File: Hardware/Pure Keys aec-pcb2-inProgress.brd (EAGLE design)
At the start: 99 x 98.7 mm, 56 parts, among them IC1 TL074P, IC5 TL074P, Q2 20MHz, T1 2N3904, U2 LM4040A50IDBZT, U3 328P

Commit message: updated in progress board added text layer text added classes for power rerouted
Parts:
- U2: value LM4040A50IDBZT -> LM4040
- moved C11 24.7 mm to (86.4, 66.0)
- moved C13 22.9 mm to (80.0, 71.1)
- moved U2 22.2 mm to (91.4, 71.1), turned to 90 degrees
- moved R4 22.2 mm to (25.4, 59.7), turned to 180 degrees
- moved C9 21.6 mm to (80.0, 66.0)
- moved IC1 21.6 mm to (31.8, 26.7)
- moved C5 20.7 mm to (47.0, 30.5)
- moved C14 19.3 mm to (31.8, 63.5)
- moved IC5 17.8 mm to (62.2, 26.7)
- moved C10 17.8 mm to (19.1, 71.1)
- moved V2 15.3 mm to (57.1, 72.4), turned to 180 degrees
- moved R21 15.3 mm to (69.8, 86.4)
- moved R3 15.2 mm to (91.4, 62.2), turned to 180 degrees
- moved C3 14.2 mm to (30.5, 49.5)
- moved R5 14.2 mm to (86.4, 22.9)
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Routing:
- net 5V: track 503.4 -> 412.2 mm, vias 0 -> 8
- net BUT2: track 27.9 -> 86.4 mm
- net GND: track 694.7 -> 641.9 mm, vias 2 -> 3
- net A1IN: track 60.0 -> 10.9 mm
- net A2IN: track 59.7 -> 10.8 mm, vias 1 -> 0
- net MK1: track 89.1 -> 41.2 mm, vias 0 -> 1
- net SCK: track 141.0 -> 99.1 mm, vias 1 -> 3
- net A0IN: track 50.3 -> 10.8 mm, vias 1 -> 0
- net MK0: track 80.1 -> 43.8 mm
- net ENOUT: track 50.5 -> 16.4 mm
- net TRIG1: track 59.8 -> 32.9 mm, vias 1 -> 0
- net N$4: track 74.9 -> 48.5 mm
- net 3VREF: track 45.8 -> 71.4 mm, vias 0 -> 1
- net MOSI: track 129.3 -> 103.8 mm, vias 0 -> 1
- net DAIN: track 41.3 -> 18.4 mm
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- removed copper zone on layer 1, net GND

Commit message: updated board and tests
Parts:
- IC1, IC5: value TL074P -> MCP6004P; device GMSN:DIL14 -> GMSN-R2Project:DIL14
- U$4: value M10X22X10_LOCK -> KeyBoard Connector
- moved ISP1 50.3 mm to (92.7, 54.6)
- moved R21 19.3 mm to (52.1, 94.0)
- moved R22 12.0 mm to (52.1, 88.9)
- moved U$4 6.48 mm to (33.0, 92.7)
- moved BUT1 6.35 mm to (61.0, 92.7)
- moved C7 5.68 mm to (90.2, 47.0), turned to 270 degrees
- moved R17 5.24 mm to (41.9, 83.8)
- moved R19 5.24 mm to (27.9, 83.8)
- moved R20 5.24 mm to (21.6, 83.8)
- moved R18 5.24 mm to (34.3, 83.8)
- moved R3 5.24 mm to (86.4, 61.0)
- moved R16 2.84 mm to (48.3, 83.8)
- moved C6 1.27 mm to (80.0, 57.1)
- moved C8 1.27 mm to (80.0, 52.1)
- moved GLIDE1 1.27 mm to (91.4, 88.9)
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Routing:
- net GND: track 641.9 -> 614.0 mm, vias 3 -> 6
- net 5V: track 412.2 -> 439.9 mm, vias 8 -> 3
- net BUT2: track 86.4 -> 59.7 mm
- net T2: track 38.0 -> 63.6 mm, vias 1 -> 0
- net T7: track 61.1 -> 36.3 mm, vias 1 -> 0
- net MISO: track 53.5 -> 29.5 mm
- net BUTLED1: track 56.8 -> 40.9 mm, vias 0 -> 1
- net T3: track 46.6 -> 62.5 mm, vias 0 -> 1
- net T6: track 50.9 -> 35.8 mm, vias 2 -> 0
- net POT1: track 61.2 -> 49.3 mm
- net MK2: track 35.2 -> 46.9 mm
- net CS2: track 35.1 -> 46.5 mm
- net MK0: track 43.8 -> 53.5 mm, vias 1 -> 0
- net N$7: track 59.5 -> 50.7 mm
- net A1OUT: track 49.5 -> 41.9 mm
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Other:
- board text added: "Pure Keys Dev Board PCB 2 AEC"
- board text removed: "Pure Keys Dev Board V0.2 AEC"

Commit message: changed 74238 for 74138
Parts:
- V1: value 74238N -> 74138N
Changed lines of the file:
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@@
 <attribute name="PROD_ID" value="IC-09136" x="54.61" y="57.15" size="1.778" layer="27" display="off"/>
 </element>
-<element name="V1" library="74ttl-din" library_urn="urn:adsk.eagle:library:84" package="DIL16" package3d_urn="urn:adsk.eagle:package:1462/1" value="74238N" x="34.29" y="72.39"/>
+<element name="V1" library="74ttl-din" library_urn="urn:adsk.eagle:library:84" package="DIL16" package3d_urn="urn:adsk.eagle:package:1462/1" value="74138N" x="34.29" y="72.39"/>
 <element name="V2" library="74ttl-din" library_urn="urn:adsk.eagle:library:84" package="DIL16" package3d_urn="urn:adsk.eagle:package:1462/1" value="74151N" x="57.15" y="72.39" rot="R180"/>
 <element name="R4" library="rcl" package="R0805" value="10K" x="25.4" y="59.69" rot="R180"/>

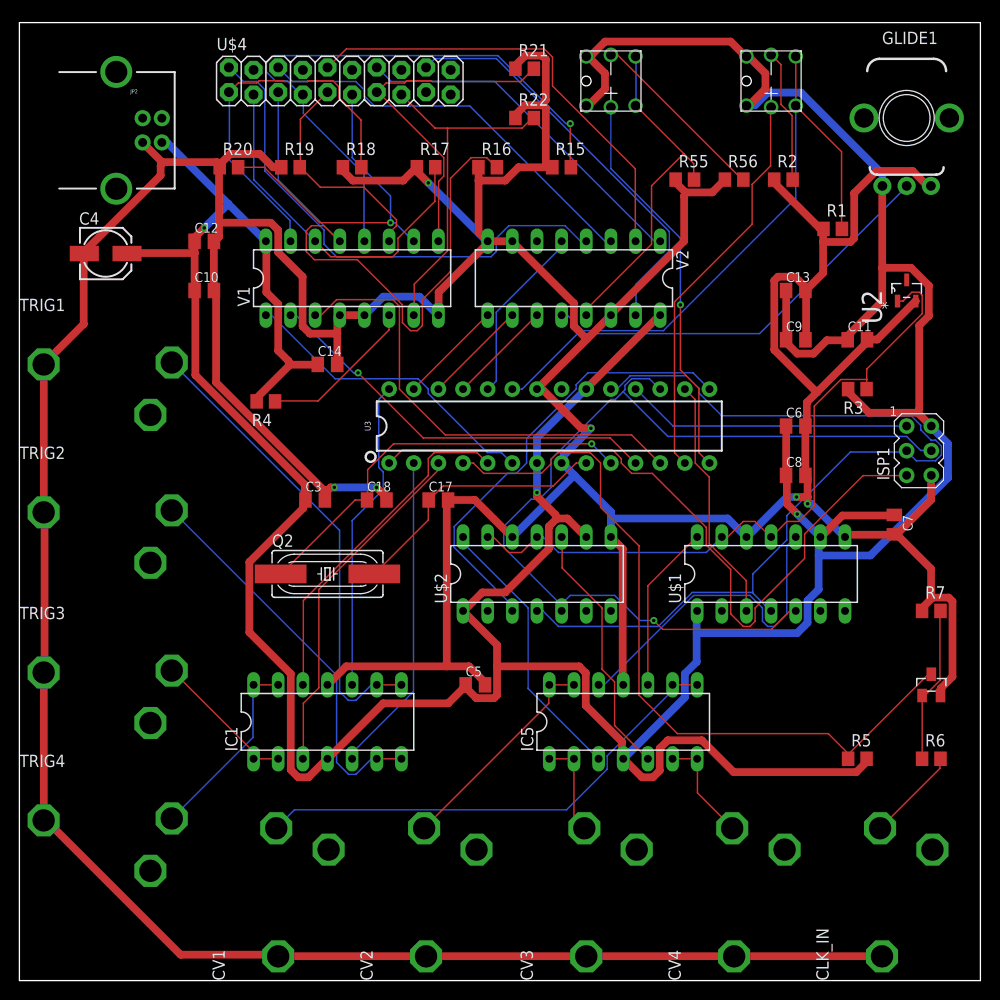
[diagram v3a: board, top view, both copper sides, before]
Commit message: updated switches on in progress
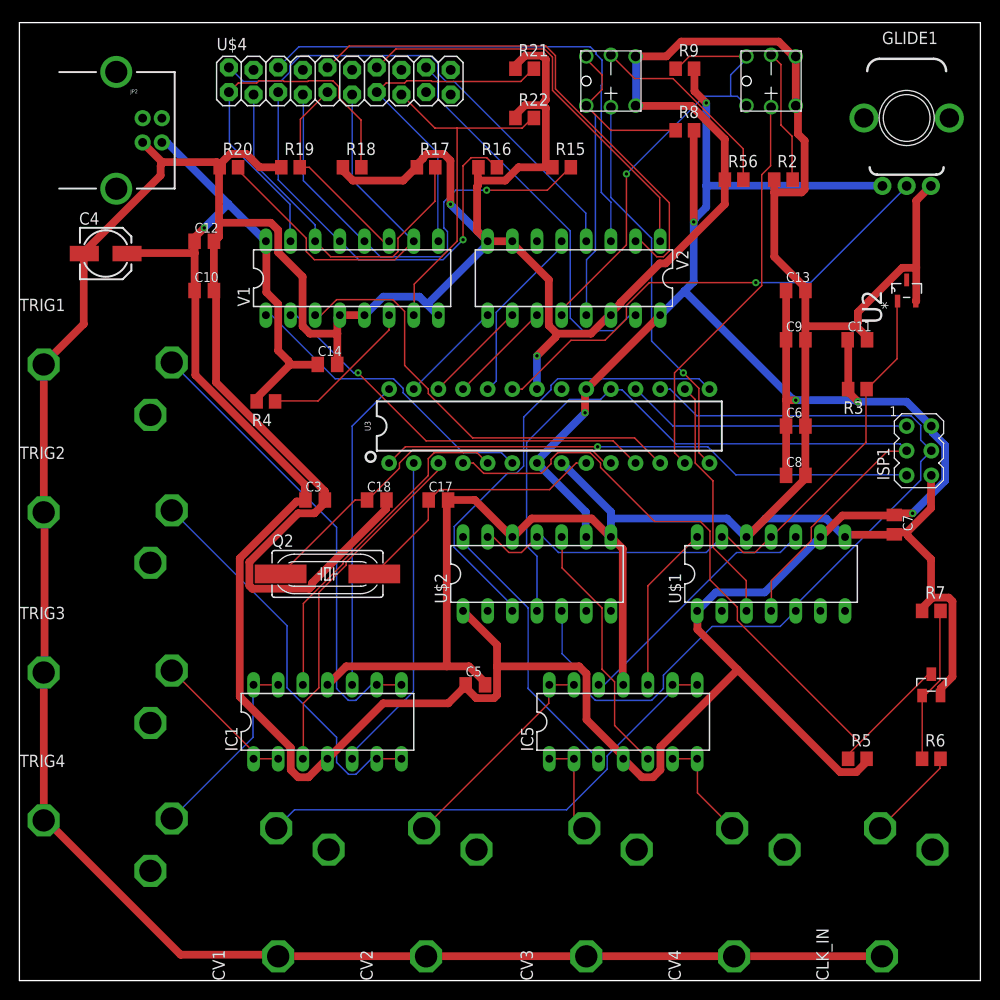
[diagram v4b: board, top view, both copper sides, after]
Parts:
- removed R1, R55: 100K, rcl:R0805
- added R8, R9: 100K, rcl:R0805
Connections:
- net 5V: now also R8.2, R9.2; no longer BUT1.3, BUT1.4, BUT2.3, BUT2.4
- net BUT1: now also BUT1.3, BUT1.4, R8.1; no longer BUT1.1, BUT1.2, R55.2
- net BUT2: now also BUT2.3, BUT2.4, R9.1; no longer BUT2.1, BUT2.2, R1.2
- net GND: now also BUT1.1, BUT1.2, BUT2.1, BUT2.2; no longer R1.1, R55.1
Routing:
- net GND: track 614.0 -> 672.2 mm, vias 6 -> 2
- net 5V: track 439.9 -> 395.9 mm, vias 3 -> 7
- net T2: track 63.6 -> 44.2 mm, vias 0 -> 1
- net RST: track 74.2 -> 55.3 mm, vias 0 -> 1
- net T3: track 62.5 -> 47.0 mm
- net BUT2: track 59.7 -> 46.1 mm, vias 0 -> 1
- net MK1: track 42.1 -> 54.0 mm
- net SCK: track 95.0 -> 85.4 mm
- net MOSI: track 97.8 -> 89.7 mm, vias 1 -> 0
- net 3VREF: track 70.9 -> 63.0 mm
- net VOUTB: track 34.2 -> 26.6 mm
- net CLK_IN: track 78.8 -> 71.3 mm
- net MK2: track 46.9 -> 54.2 mm
- net MK3: track 36.7 -> 42.8 mm
- net T5: track 36.1 -> 41.6 mm, vias 1 -> 0
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
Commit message: Updated routing on in-progress board to make room for 1K pull downs
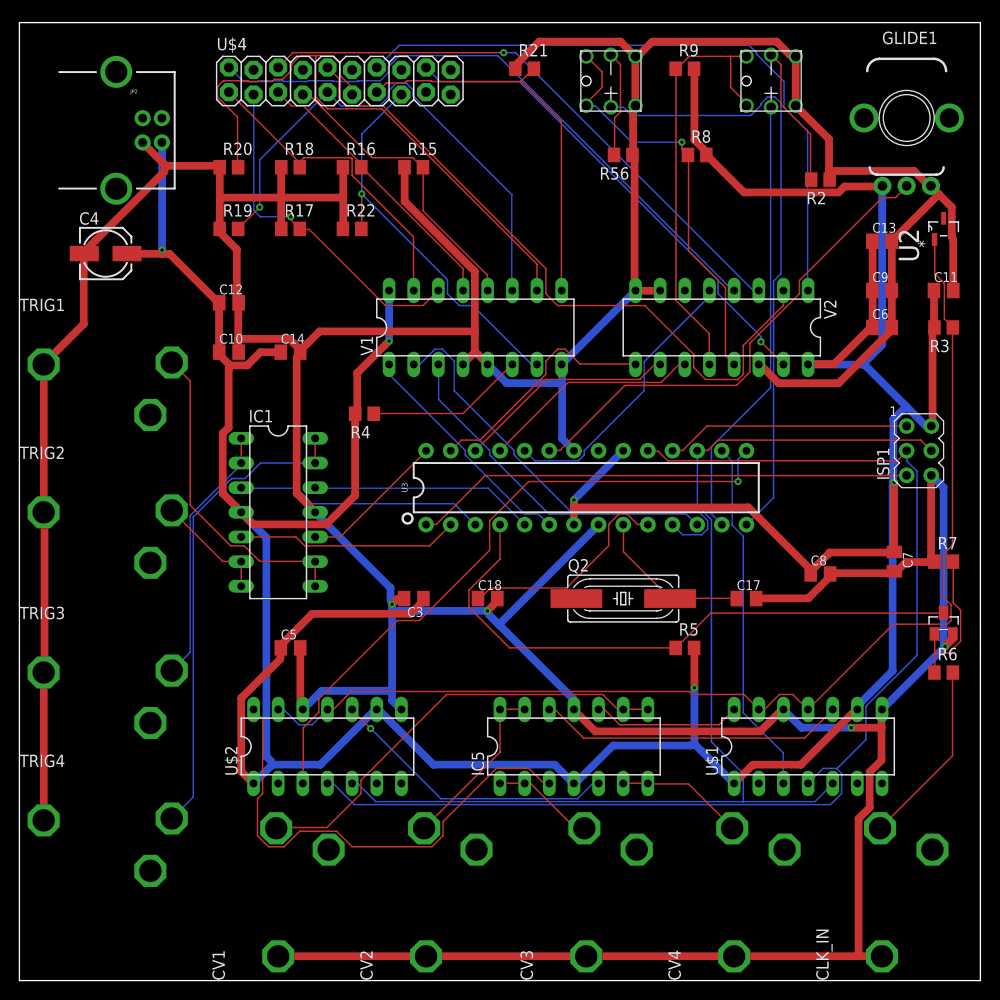
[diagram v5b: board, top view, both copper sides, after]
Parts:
- moved C17 33.3 mm to (74.9, 39.4)
- moved Q2 30.6 mm to (62.2, 39.4)
- moved U$2 28.0 mm to (31.8, 24.1)
- moved IC1 22.2 mm to (26.7, 48.3), turned to 270 degrees
- moved R22 21.1 mm to (34.3, 77.5)
- moved R5 21.1 mm to (68.6, 34.3)
- moved C5 19.4 mm to (27.9, 34.3)
- moved U$1 18.2 mm to (81.3, 24.1)
- moved V2 16.1 mm to (72.4, 67.3)
- moved R17 15.3 mm to (27.9, 77.5)
- moved C18 15.3 mm to (48.3, 39.4)
- moved R15 15.2 mm to (40.6, 83.8)
- moved C3 14.4 mm to (40.6, 39.4), turned to 180 degrees
- moved R16 14.0 mm to (34.3, 83.8)
- moved V1 13.7 mm to (47.0, 67.3)
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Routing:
- net GND: track 672.2 -> 616.6 mm, vias 2 -> 4
- net 3VREF: track 63.0 -> 118.1 mm
- net SCK: track 85.4 -> 125.0 mm
- net T4: track 21.3 -> 53.9 mm, vias 0 -> 1
- net N$5: track 19.8 -> 49.4 mm
- net N$3: track 40.9 -> 11.9 mm
- net MOSI: track 89.7 -> 114.3 mm
- net MK3: track 42.8 -> 67.1 mm
- net BUTLED1: track 40.9 -> 64.0 mm, vias 1 -> 0
- net T5: track 41.6 -> 64.5 mm
- net VOUTC: track 28.7 -> 50.3 mm
- net 5V: track 395.9 -> 416.2 mm, vias 7 -> 5
- net CS2: track 47.5 -> 67.2 mm, vias 0 -> 1
- net TRIG1: track 32.1 -> 15.1 mm
- net T3: track 47.0 -> 30.9 mm, vias 1 -> 0
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
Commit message: changed in progress board
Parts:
- added R1, R10, R11, R12, R13: 1K, rcl:R0805
- R3: value 10K -> 2K
- U2: device GMSN:SOT95P237X112-3N -> GMSN-R2Project:SOT95P237X112-3N
- V1: value 74138N -> 74238N
- moved C11 37.4 mm to (88.9, 34.3)
- moved U2 36.6 mm to (82.5, 43.2)
- moved R3 35.4 mm to (82.5, 34.3)
- moved C9 23.7 mm to (82.5, 48.3)
- moved C6 11.7 mm to (81.3, 58.4)
- moved C8 10.8 mm to (74.9, 34.3)
- moved C13 6.48 mm to (82.5, 77.5)
- moved ISP1 4.02 mm to (94.0, 58.4)
- moved C7 1.27 mm to (90.2, 44.5)
- moved R7 1.27 mm to (95.2, 44.5)
- moved T1 1.27 mm to (95.2, 38.1)
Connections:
- net GND: now also R1.1, R10.1, R11.1, R12.1, R13.1
- net MK0: now also R1.2
- net MK1: now also R10.2
- net MK2: now also R11.2
- net MK3: now also R12.2
- net MK4: now also R13.2
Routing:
- net GND: track 616.6 -> 674.9 mm, vias 4 -> 9
- net 3VREF: track 118.1 -> 80.4 mm, vias 0 -> 1
- net 5V: track 416.2 -> 400.0 mm
- net BUT1: track 43.0 -> 58.6 mm, vias 1 -> 0
- net MK4: track 50.6 -> 62.6 mm, vias 1 -> 0
- net BUTLED1: track 64.0 -> 53.2 mm, vias 0 -> 2
- net A0IN: track 22.8 -> 33.5 mm
- net MOSI: track 114.3 -> 123.0 mm
- net CS2: track 67.2 -> 75.7 mm, vias 1 -> 0
- net T5: track 64.5 -> 57.8 mm
- net VOUTC: track 50.3 -> 43.8 mm
- net T0: track 33.1 -> 39.5 mm
- net T4: track 53.9 -> 48.6 mm
- net VOUTD: track 29.9 -> 35.0 mm, vias 1 -> 0
- net N$7: track 45.5 -> 50.5 mm
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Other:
- board text added: "KeyBoard Controller"
- board text added: "Pure Keys Dev Board PCB 2 GMSN! and Andy C"
- board text removed: "Pure Keys Dev Board PCB 2 AEC"
